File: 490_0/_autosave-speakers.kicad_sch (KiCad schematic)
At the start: 9 parts, among them J15 Conn_01x07, J16 Conn_01x10, J20 S2B-XH-A, U9 MAX98357A

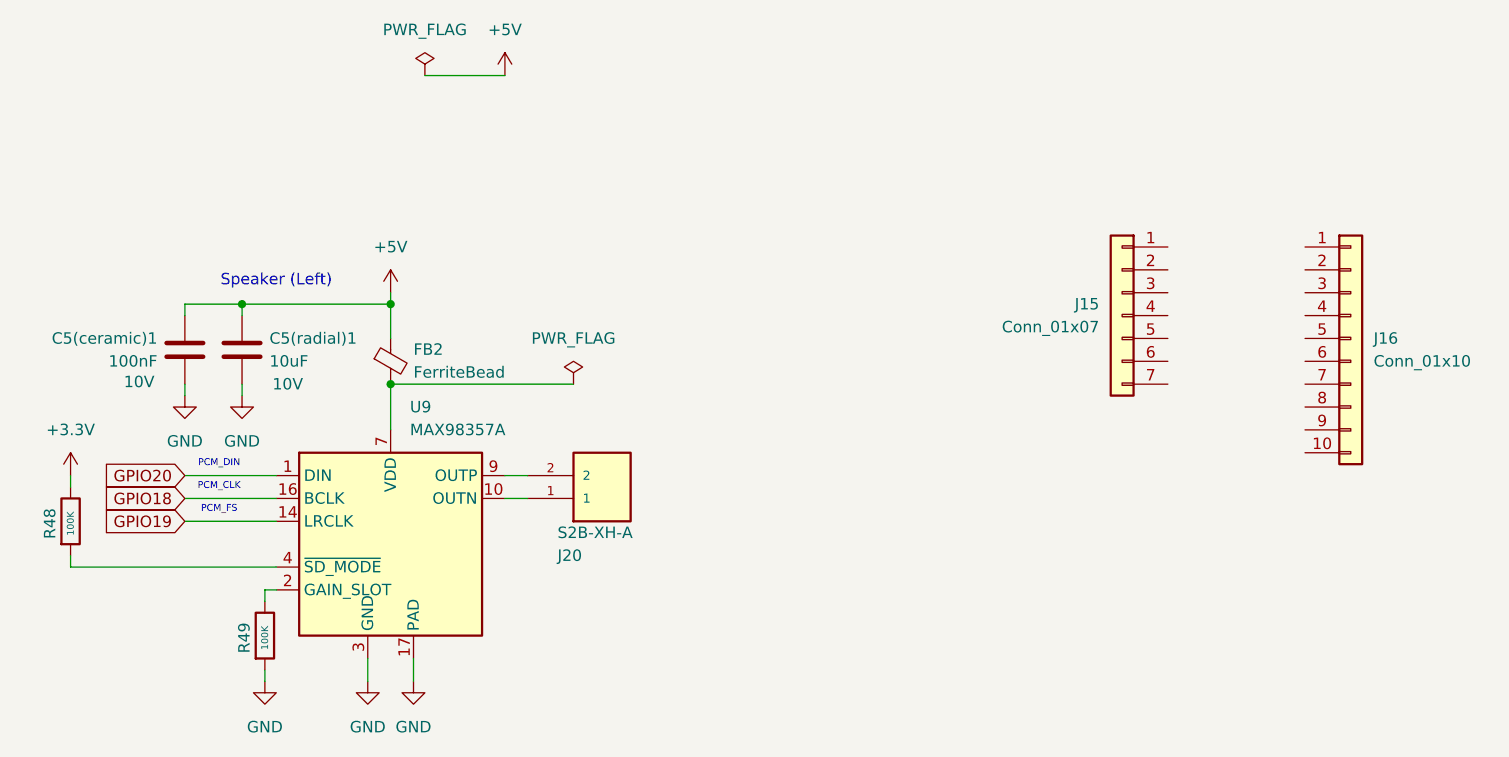
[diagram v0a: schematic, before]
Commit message: Changed PCB block dagram and layout
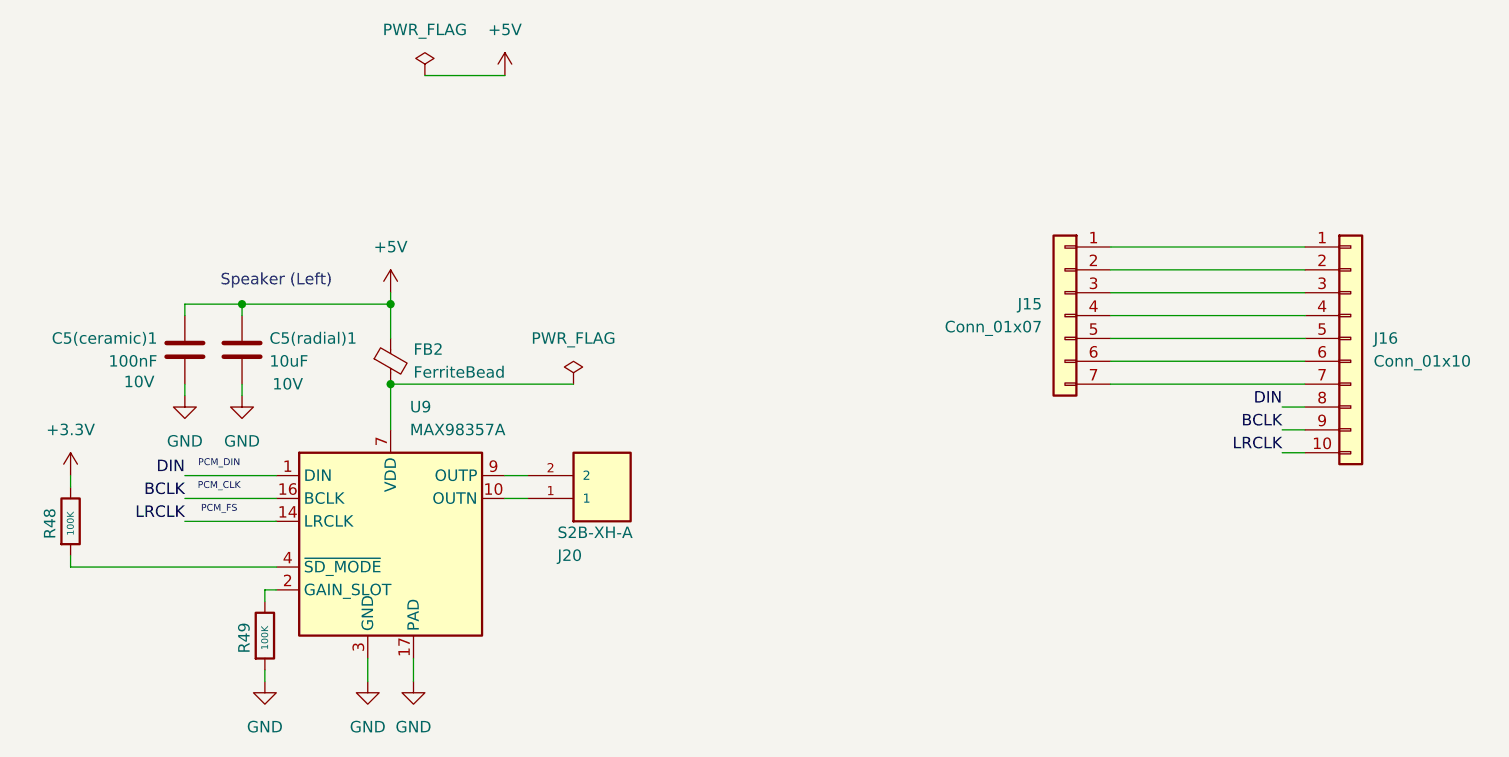
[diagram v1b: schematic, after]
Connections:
- net GPIO18 is gone; now on net BCLK: U9.16 (BCLK)
- net GPIO19 is gone; now on net LRCLK: U9.14 (LRCLK)
- net GPIO20 is gone; now on net DIN: U9.1 (DIN)
- net at J15.1 (Pin_1): now also J16.1 (Pin_1)
- net at J15.2 (Pin_2): now also J16.2 (Pin_2)
- net at J15.3 (Pin_3): now also J16.3 (Pin_3)
- net at J15.4 (Pin_4): now also J16.4 (Pin_4)
- net at J15.5 (Pin_5): now also J16.5 (Pin_5)
- net at J15.6 (Pin_6): now also J16.6 (Pin_6)
- net at J15.7 (Pin_7): now also J16.7 (Pin_7)
- net LRCLK: now reaches J16.10 (Pin_10)
- net DIN: now reaches J16.8 (Pin_8)
- net BCLK: now reaches J16.9 (Pin_9)
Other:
- moved on the sheet: J15
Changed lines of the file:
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@@
+	(wire
+		(pts
+			(xy 194.31 86.36) (xy 215.9 86.36)
+		)
+		(stroke
+			(width 0)
+			(type default)
+		)
+	)
 	(wire
 		(pts
@@
 	(wire
 		(pts
+			(xy 194.31 73.66) (xy 215.9 73.66)
+		)
+		(stroke
+			(width 0)
+			(type default)
+		)
+	)
+	(wire
+		(pts
+			(xy 213.36 96.52) (xy 215.9 96.52)
+		)
+		(stroke
+			(width 0)
+			(type default)
+		)
+	)
+	(wire
+		(pts
+			(xy 194.31 78.74) (xy 215.9 78.74)
+		)
+		(stroke
+			(width 0)
+			(type default)
+		)
+	)
+	(wire
+		(pts
 			(xy 100.33 121.92) (xy 100.33 120.65)
 		)
@@
 	(wire
 		(pts
+			(xy 194.31 76.2) (xy 215.9 76.2)
+		)
+		(stroke
+			(width 0)
+			(type default)
+		)
+	)
+	(wire
+		(pts
 			(xy 91.44 81.28) (xy 91.44 80.01)
 		)
@@
 	(wire
 		(pts
+			(xy 194.31 81.28) (xy 215.9 81.28)
+		)
+		(stroke
+			(width 0)
+			(type default)
+		)
+	)
+	(wire
+		(pts
 			(xy 114.3 88.9) (xy 114.3 93.98)
 		)
@@
 	(wire
 		(pts
+			(xy 194.31 88.9) (xy 215.9 88.9)
+		)
+		(stroke
+			(width 0)
+			(type default)
+		)
+	)
+	(wire
+		(pts
+			(xy 213.36 91.44) (xy 215.9 91.44)
+		)
+		(stroke
+			(width 0)
+			(type default)
+		)
+	)
+	(wire
+		(pts
+			(xy 194.31 83.82) (xy 215.9 83.82)
+		)
+		(stroke
+			(width 0)
+			(type default)
+		)
+	)
+	(wire
+		(pts
 			(xy 78.74 109.22) (xy 78.74 107.95)
 		)
@@
 	(wire
 		(pts
+			(xy 213.36 93.98) (xy 215.9 93.98)
+		)
+		(stroke
+			(width 0)
+			(type default)
+		)
+	)
+	(wire
+		(pts
 			(xy 111.76 119.38) (xy 111.76 121.92)
 		)
@@
 		)
 	)
-	(global_label "GPIO18"
-		(shape input)
+	(label "BCLK"
+		(at 213.36 93.98 180)
+		(effects
+			(font
+				(size 1.27 1.27)
+			)
+			(justify right bottom)
+		)
+	)
+	(label "BCLK"
 		(at 91.44 101.6 180)
 		(effects
@@
 				(size 1.27 1.27)
 			)
-			(justify right)
-		)
-		(property "Intersheetrefs" "${INTERSHEET_REFS}"
-			(at 91.44 101.6 0)
-			(effects
-				(font
-					(size 1.27 1.27)
-				)
-				(hide yes)
-			)
-		)
-	)
-	(global_label "GPIO19"
-		(shape input)
+			(justify right bottom)
+		)
+	)
+	(label "LRCLK"
 		(at 91.44 104.14 180)
 		(effects
@@
 				(size 1.27 1.27)
 			)
-			(justify right)
-		)
-		(property "Intersheetrefs" "${INTERSHEET_REFS}"
-			(at 91.44 104.14 0)
-			(effects
-				(font
-					(size 1.27 1.27)
-				)
-				(justify left)
-				(hide yes)
-			)
-		)
-	)
-	(global_label "GPIO20"
-		(shape input)
+			(justify right bottom)
+		)
+	)
+	(label "LRCLK"
+		(at 213.36 96.52 180)
+		(effects
+			(font
+				(size 1.27 1.27)
+			)
+			(justify right bottom)
+		)
+	)
+	(label "DIN"
 		(at 91.44 99.06 180)
 		(effects
@@
 				(size 1.27 1.27)
 			)
-			(justify right)
-		)
-		(property "Intersheetrefs" "${INTERSHEET_REFS}"
-			(at 91.44 99.06 0)
-			(effects
-				(font
-					(size 1.27 1.27)
-				)
-				(hide yes)
-			)
+			(justify right bottom)
+		)
+	)
+	(label "DIN"
+		(at 213.36 91.44 180)
+		(effects
+			(font
+				(size 1.27 1.27)
+			)
+			(justify right bottom)
 		)
 	)
@@
 	(symbol
 		(lib_id "Connector_Generic:Conn_01x07")
-		(at 195.58 81.28 0)
+		(at 189.23 81.28 0)
 		(mirror y)
 		(unit 1)
@@
 		(dnp no)
 		(property "Reference" "J15"
-			(at 193.04 80.0099 0)
+			(at 186.69 80.0099 0)
 			(effects
 				(font
@@
 		)
 		(property "Value" "Conn_01x07"
-			(at 193.04 82.5499 0)
+			(at 186.69 82.5499 0)
 			(effects
 				(font
@@
 		)
 		(property "Footprint" ""
-			(at 195.58 81.28 0)
+			(at 189.23 81.28 0)
 			(effects
 				(font
@@
 		)
 		(property "Datasheet" "~"
-			(at 195.58 81.28 0)
+			(at 189.23 81.28 0)
 			(effects
 				(font
@@
 		)
 		(property "Description" "Generic connector, single row, 01x07, script generated (kicad-library-utils/schlib/autogen/connector/)"
-			(at 195.58 81.28 0)
-			(effects
-				(font
+			(at 189.23 81.28 0)
+			(effects
+				(font
